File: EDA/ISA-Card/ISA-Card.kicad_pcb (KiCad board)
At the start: 2 copper layers, 138.4 x 98.4 mm, 53 parts, among them U7101 74HCT245, U7102 74HCT244, U7104 74HCT138, U7105 74HCT138, U7106 74LS08, U7107 74LS32, U7108 74LS32, U7109 74HC368, U7110 74HC04, U7111 74HC125, U7112 74HC74, U7113 74HC74, U7114 74HC4024, U7115 74HC4024, U7116 74HC595, U7117 74HC595, U7118 74HC595, U7119 8251, U7120 26LS31, U7121 26LS32, X2 Conn_02x04_Counter_Clockwise, X3 DB15_Female, X5 Conn_02x08_Counter_Clockwise

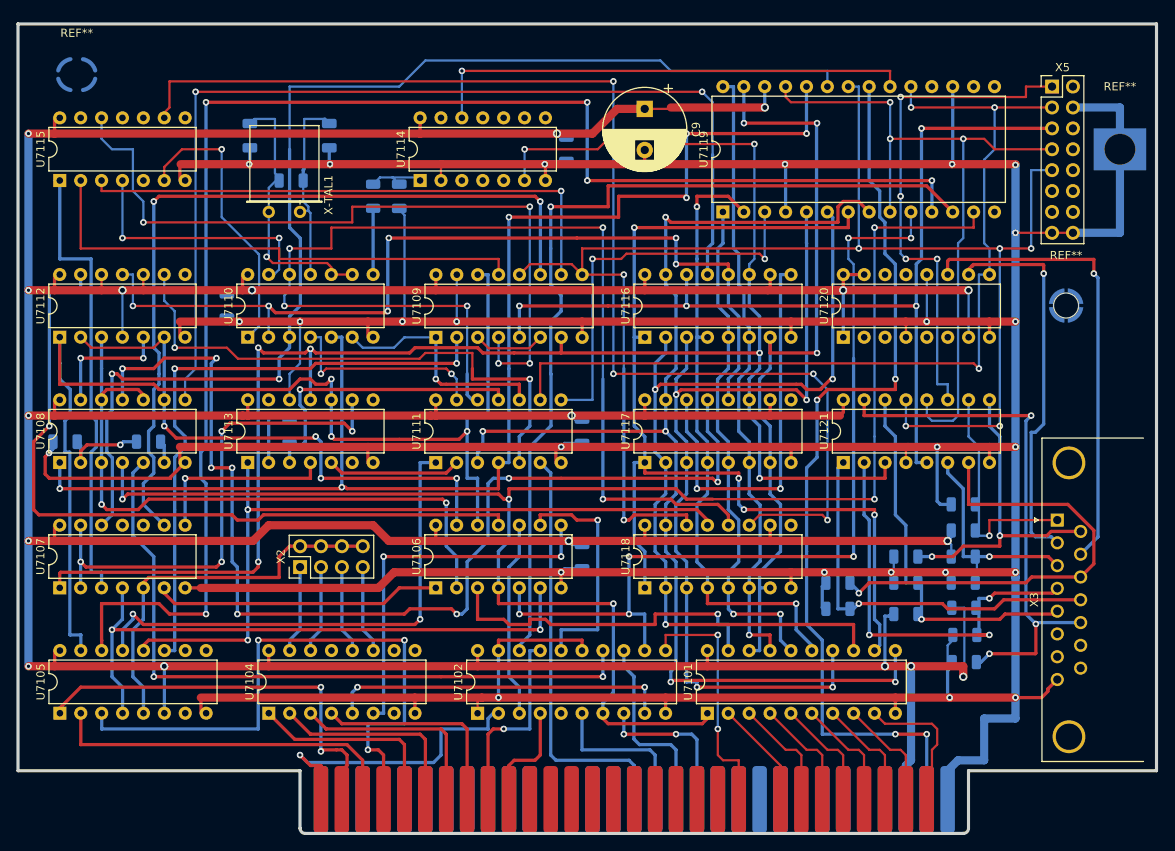
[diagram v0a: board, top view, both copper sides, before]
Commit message: Added test points
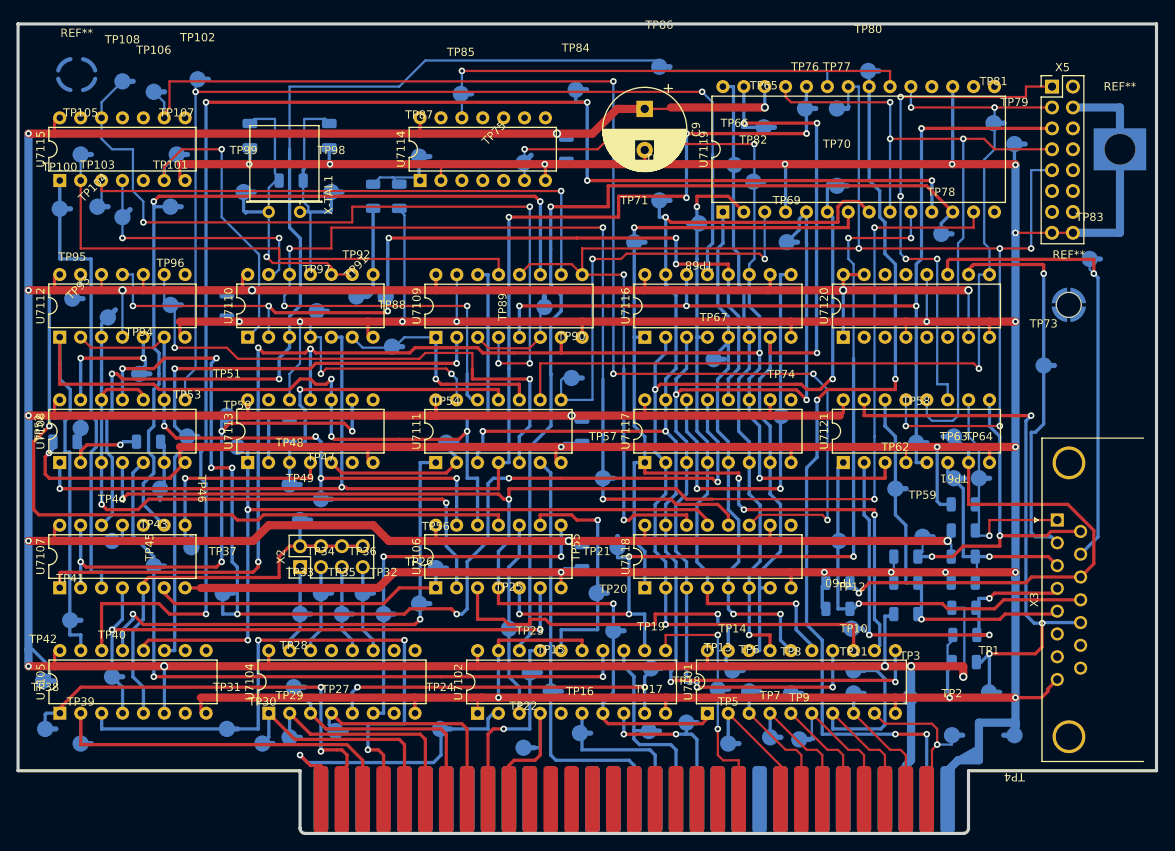
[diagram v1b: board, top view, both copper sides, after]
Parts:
- added TP1: TestPoint, Philips-Shapes:Test Point, F.Cu at (190.4, 132.7)
- added TP10: TestPoint, Philips-Shapes:Test Point, F.Cu at (174.0, 130.0)
- added TP100: TestPoint, Philips-Shapes:Test Point, F.Cu at (77.5, 73.9)
- added TP101: TestPoint, Philips-Shapes:Test Point, F.Cu at (90.9, 73.7)
- added TP102: TestPoint, Philips-Shapes:Test Point, F.Cu at (94.2, 58.2)
- added TP103: TestPoint, Philips-Shapes:Test Point, F.Cu at (82.0, 73.7)
- added TP104: TestPoint, Philips-Shapes:Test Point, F.Cu at (85.1, 74.9)
- added TP105: TestPoint, Philips-Shapes:Test Point, F.Cu at (80.0, 67.3)
- added TP106: TestPoint, Philips-Shapes:Test Point, F.Cu at (88.9, 59.7)
- added TP107: TestPoint, Philips-Shapes:Test Point, F.Cu at (91.7, 67.3)
- added TP108: TestPoint, Philips-Shapes:Test Point, F.Cu at (85.1, 58.4)
- added TP11: TestPoint, Philips-Shapes:Test Point, F.Cu at (174.0, 132.8)
- added TP12: TestPoint, Philips-Shapes:Test Point, F.Cu at (173.7, 125.0)
- added TP13: TestPoint, Philips-Shapes:Test Point, F.Cu at (157.5, 132.3)
- added TP14: TestPoint, Philips-Shapes:Test Point, F.Cu at (159.3, 130.0)
- added TP15: TestPoint, Philips-Shapes:Test Point, F.Cu at (137.2, 132.6)
- added TP16: TestPoint, Philips-Shapes:Test Point, F.Cu at (140.7, 137.7)
- added TP17: TestPoint, Philips-Shapes:Test Point, F.Cu at (149.1, 137.4)
- added TP18: TestPoint, Philips-Shapes:Test Point, F.Cu at (153.7, 136.4)
- added TP19: TestPoint, Philips-Shapes:Test Point, F.Cu at (149.4, 129.8)
- added TP2: TestPoint, Philips-Shapes:Test Point, F.Cu at (185.9, 137.9)
- added TP20: TestPoint, Philips-Shapes:Test Point, F.Cu at (144.8, 125.2)
- added TP21: TestPoint, Philips-Shapes:Test Point, F.Cu at (142.7, 120.7)
- added TP22: TestPoint, Philips-Shapes:Test Point, F.Cu at (133.9, 139.4)
- added TP23: TestPoint, Philips-Shapes:Test Point, F.Cu at (134.6, 130.3)
- added TP24: TestPoint, Philips-Shapes:Test Point, F.Cu at (123.7, 137.2)
- added TP25: TestPoint, Philips-Shapes:Test Point, F.Cu at (132.1, 125.0)
- added TP26: TestPoint, Philips-Shapes:Test Point, F.Cu at (121.2, 121.9)
- added TP27: TestPoint, Philips-Shapes:Test Point, F.Cu at (111.0, 137.4)
- added TP28: TestPoint, Philips-Shapes:Test Point, F.Cu at (105.9, 132.1)
- added TP29: TestPoint, Philips-Shapes:Test Point, F.Cu at (105.4, 138.2)
- added TP3: TestPoint, Philips-Shapes:Test Point, F.Cu at (180.8, 133.3)
- added TP30: TestPoint, Philips-Shapes:Test Point, F.Cu at (102.1, 138.9)
- added TP31: TestPoint, Philips-Shapes:Test Point, F.Cu at (97.8, 137.2)
- added TP32: TestPoint, Philips-Shapes:Test Point, F.Cu at (116.8, 123.2)
- added TP33: TestPoint, Philips-Shapes:Test Point, F.Cu at (106.7, 123.2)
- added TP34: TestPoint, Philips-Shapes:Test Point, F.Cu at (109.2, 120.7)
- added TP35: TestPoint, Philips-Shapes:Test Point, F.Cu at (111.8, 123.2)
- added TP36: TestPoint, Philips-Shapes:Test Point, F.Cu at (114.3, 120.7)
- added TP37: TestPoint, Philips-Shapes:Test Point, F.Cu at (97.3, 120.7)
- added TP38: TestPoint, Philips-Shapes:Test Point, F.Cu at (75.7, 137.2)
- added TP39: TestPoint, Philips-Shapes:Test Point, F.Cu at (80.0, 138.9)
- added TP4: TestPoint, Philips-Shapes:Test Point, F.Cu at (193.5, 137.9)
- added TP40: TestPoint, Philips-Shapes:Test Point, F.Cu at (83.8, 130.8)
- added TP41: TestPoint, Philips-Shapes:Test Point, F.Cu at (78.7, 124.0)
- added TP42: TestPoint, Philips-Shapes:Test Point, F.Cu at (75.4, 131.3)
- added TP43: TestPoint, Philips-Shapes:Test Point, F.Cu at (88.9, 117.3)
- added TP44: TestPoint, Philips-Shapes:Test Point, F.Cu at (83.8, 114.3)
- added TP45: TestPoint, Philips-Shapes:Test Point, F.Cu at (93.5, 115.1)
- added TP46: TestPoint, Philips-Shapes:Test Point, F.Cu at (89.7, 108.0)
- added TP47: TestPoint, Philips-Shapes:Test Point, F.Cu at (109.2, 109.2)
- added TP48: TestPoint, Philips-Shapes:Test Point, F.Cu at (105.4, 107.4)
- added TP49: TestPoint, Philips-Shapes:Test Point, F.Cu at (106.7, 111.8)
- added TP5: TestPoint, Philips-Shapes:Test Point, F.Cu at (158.8, 138.9)
- added TP50: TestPoint, Philips-Shapes:Test Point, F.Cu at (99.1, 102.9)
- added TP51: TestPoint, Philips-Shapes:Test Point, F.Cu at (97.8, 99.1)
- added TP52: TestPoint, Philips-Shapes:Test Point, F.Cu at (80.0, 100.6)
- added TP53: TestPoint, Philips-Shapes:Test Point, F.Cu at (93.0, 101.6)
- added TP54: TestPoint, Philips-Shapes:Test Point, F.Cu at (124.5, 102.4)
- added TP55: TestPoint, Philips-Shapes:Test Point, F.Cu at (145.3, 115.1)
- added TP56: TestPoint, Philips-Shapes:Test Point, F.Cu at (123.2, 117.6)
- added TP57: TestPoint, Philips-Shapes:Test Point, F.Cu at (143.5, 106.7)
- added TP58: TestPoint, Philips-Shapes:Test Point, F.Cu at (181.6, 102.4)
- added TP59: TestPoint, Philips-Shapes:Test Point, F.Cu at (182.4, 113.8)
- added TP6: TestPoint, Philips-Shapes:Test Point, F.Cu at (161.3, 132.6)
- added TP60: TestPoint, Philips-Shapes:Test Point, F.Cu at (172.2, 114.3)
- added TP61: TestPoint, Philips-Shapes:Test Point, F.Cu at (186.2, 101.6)
- added TP62: TestPoint, Philips-Shapes:Test Point, F.Cu at (179.1, 108.0)
- added TP63: TestPoint, Philips-Shapes:Test Point, F.Cu at (186.2, 106.7)
- added TP64: TestPoint, Philips-Shapes:Test Point, F.Cu at (189.2, 106.7)
- added TP65: TestPoint, Philips-Shapes:Test Point, F.Cu at (163.1, 64.0)
- added TP66: TestPoint, Philips-Shapes:Test Point, F.Cu at (159.5, 68.6)
- added TP67: TestPoint, Philips-Shapes:Test Point, F.Cu at (157.0, 92.2)
- added TP68: TestPoint, Philips-Shapes:Test Point, F.Cu at (155.2, 75.7)
- added TP69: TestPoint, Philips-Shapes:Test Point, F.Cu at (165.9, 78.0)
- added TP7: TestPoint, Philips-Shapes:Test Point, F.Cu at (163.8, 138.2)
- added TP70: TestPoint, Philips-Shapes:Test Point, F.Cu at (172.0, 71.1)
- added TP71: TestPoint, Philips-Shapes:Test Point, F.Cu at (147.3, 78.0)
- added TP72: TestPoint, Philips-Shapes:Test Point, F.Cu at (150.4, 72.9)
- added TP73: TestPoint, Philips-Shapes:Test Point, F.Cu at (197.1, 93.0)
- added TP74: TestPoint, Philips-Shapes:Test Point, F.Cu at (165.2, 99.1)
- added TP75: TestPoint, Philips-Shapes:Test Point, F.Cu at (133.9, 68.3)
- added TP76: TestPoint, Philips-Shapes:Test Point, F.Cu at (168.1, 61.7)
- added TP77: TestPoint, Philips-Shapes:Test Point, F.Cu at (172.0, 61.7)
- added TP78: TestPoint, Philips-Shapes:Test Point, F.Cu at (184.7, 77.0)
- added TP79: TestPoint, Philips-Shapes:Test Point, F.Cu at (193.5, 66.0)
- added TP8: TestPoint, Philips-Shapes:Test Point, F.Cu at (166.4, 132.8)
- added TP80: TestPoint, Philips-Shapes:Test Point, F.Cu at (175.8, 57.1)
- added TP81: TestPoint, Philips-Shapes:Test Point, F.Cu at (191.0, 63.5)
- added TP82: TestPoint, Philips-Shapes:Test Point, F.Cu at (161.8, 70.6)
- added TP83: TestPoint, Philips-Shapes:Test Point, F.Cu at (202.7, 80.0)
- added TP84: TestPoint, Philips-Shapes:Test Point, F.Cu at (140.2, 59.4)
- added TP85: TestPoint, Philips-Shapes:Test Point, F.Cu at (126.2, 59.9)
- added TP86: TestPoint, Philips-Shapes:Test Point, F.Cu at (150.4, 56.6)
- added TP87: TestPoint, Philips-Shapes:Test Point, F.Cu at (121.2, 67.6)
- added TP88: TestPoint, Philips-Shapes:Test Point, F.Cu at (117.9, 90.7)
- added TP89: TestPoint, Philips-Shapes:Test Point, F.Cu at (136.4, 85.9)
- added TP9: TestPoint, Philips-Shapes:Test Point, F.Cu at (167.4, 138.4)
- added TP90: TestPoint, Philips-Shapes:Test Point, F.Cu at (139.7, 94.5)
- added TP91: TestPoint, Philips-Shapes:Test Point, F.Cu at (117.1, 84.6)
- added TP92: TestPoint, Philips-Shapes:Test Point, F.Cu at (113.5, 84.6)
- added TP93: TestPoint, Philips-Shapes:Test Point, F.Cu at (83.3, 87.1)
- added TP94: TestPoint, Philips-Shapes:Test Point, F.Cu at (87.1, 94.0)
- added TP95: TestPoint, Philips-Shapes:Test Point, F.Cu at (79.0, 84.8)
- added TP96: TestPoint, Philips-Shapes:Test Point, F.Cu at (90.9, 85.6)
- added TP97: TestPoint, Philips-Shapes:Test Point, F.Cu at (108.7, 86.4)
- added TP98: TestPoint, Philips-Shapes:Test Point, F.Cu at (110.5, 71.9)
- added TP99: TestPoint, Philips-Shapes:Test Point, F.Cu at (99.8, 71.9)
- moved REF** 0.34 mm to (200.2, 85.6)
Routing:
- net /D5: track 13.9 -> 31.1 mm
- net Net-(C5-Pad2): track 23.7 -> 29.8 mm
- net VCC: track 726.7 -> 732.5 mm
- net Net-(C6-Pad2): track 32.9 -> 38.4 mm
- net Net-(U7109-Pad4): track 91.2 -> 96.7 mm
- net /A9: track 13.5 -> 18.8 mm
- net /MDB3: track 106.3 -> 111.1 mm
- net /MDB4: track 106.4 -> 111.1 mm
- net Net-(R3-Pad2): track 8.05 -> 12.5 mm
- net /Attention-: track 65.1 -> 69.5 mm
- net Net-(TP37-Pad1): track 133.9 -> 138.2 mm
- net /D4: track 13.9 -> 17.9 mm
- net /Data-: track 57.5 -> 61.5 mm
- net /A4: track 24.8 -> 28.8 mm
- net /A6: track 25.5 -> 29.5 mm
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
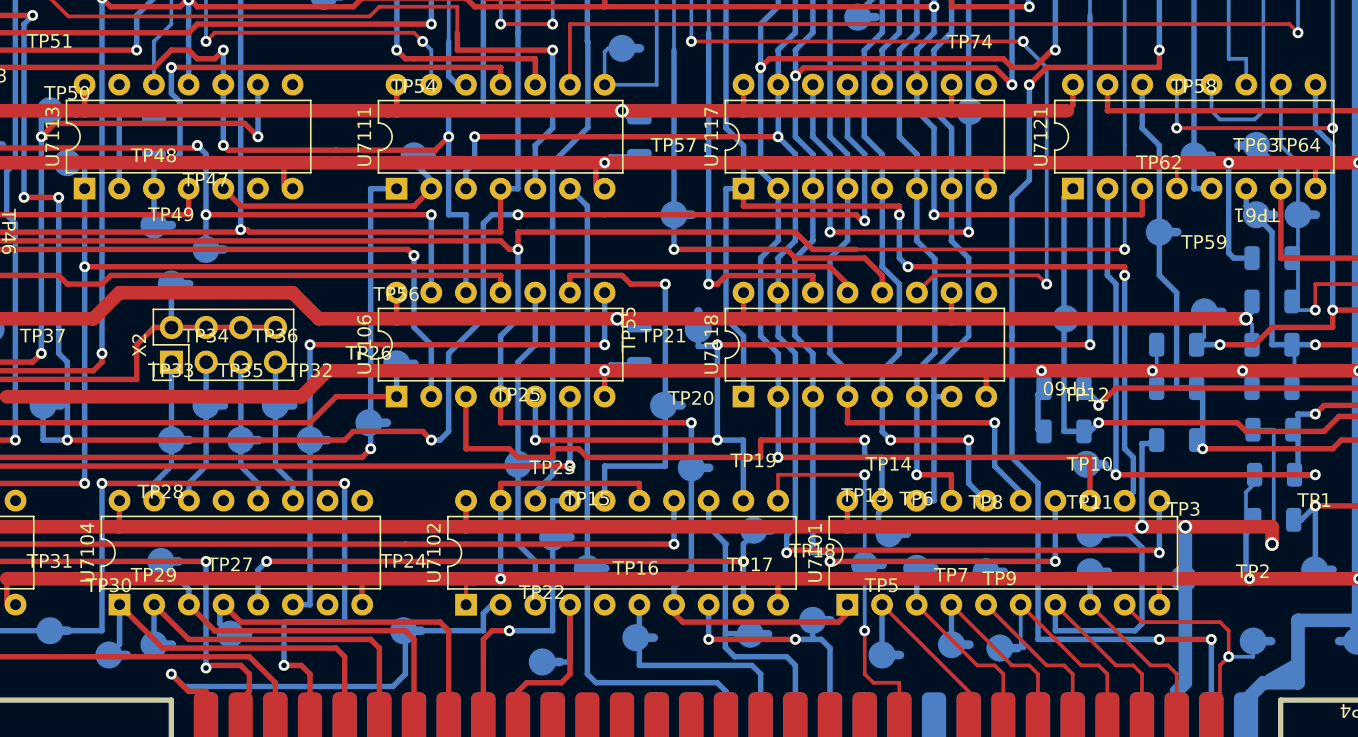
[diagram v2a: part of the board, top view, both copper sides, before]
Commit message: Fixed missed connection on 7113 Pin 13
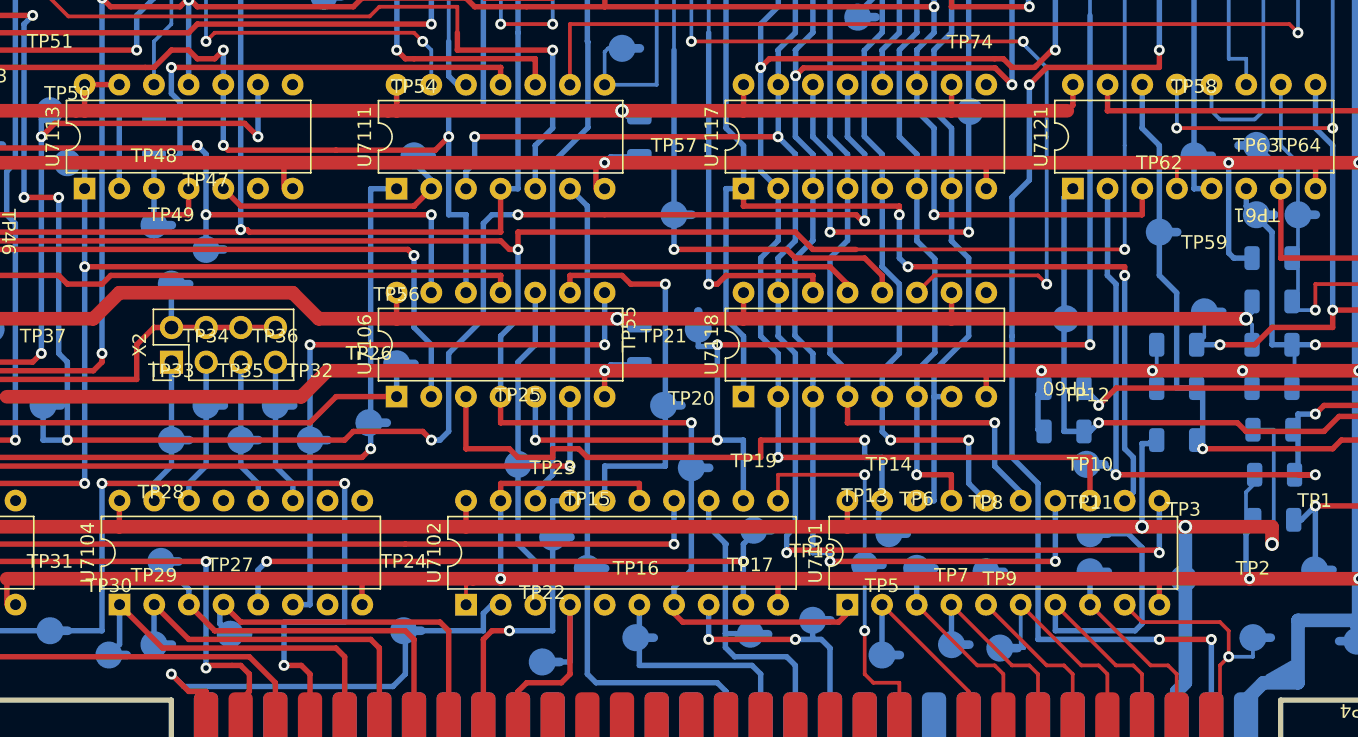
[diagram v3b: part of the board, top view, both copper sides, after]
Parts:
- moved TP2 0.25 mm to (185.9, 137.7)
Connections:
- net /Data Clock HV renamed /CLKp3
- net /Port Selection renamed /IOSEL
- net Net-(R4-Pad2) renamed /DMA_READ
- net Net-(TP19-Pad1) renamed /AENb
- net Net-(TP20-Pad1) renamed /~{RD}
- net Net-(TP21-Pad1) renamed /A9b
- net Net-(TP25-Pad1) renamed /A8b
- net Net-(TP40-Pad1) renamed /IOACT
- net Net-(TP43-Pad1) renamed /DMA_ACK
- net Net-(TP55-Pad1) renamed /~{WR}
- net Net-(U7102-Pad18) renamed /A0b
- net Net-(U7108-Pad1) renamed /~{DTR}
- net Net-(U7114-Pad12) renamed /CLKp0
- U7113 pad 13: unconnected-(U7113-Pad13) -> VCC
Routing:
- net VCC: track 732.5 -> 735.0 mm

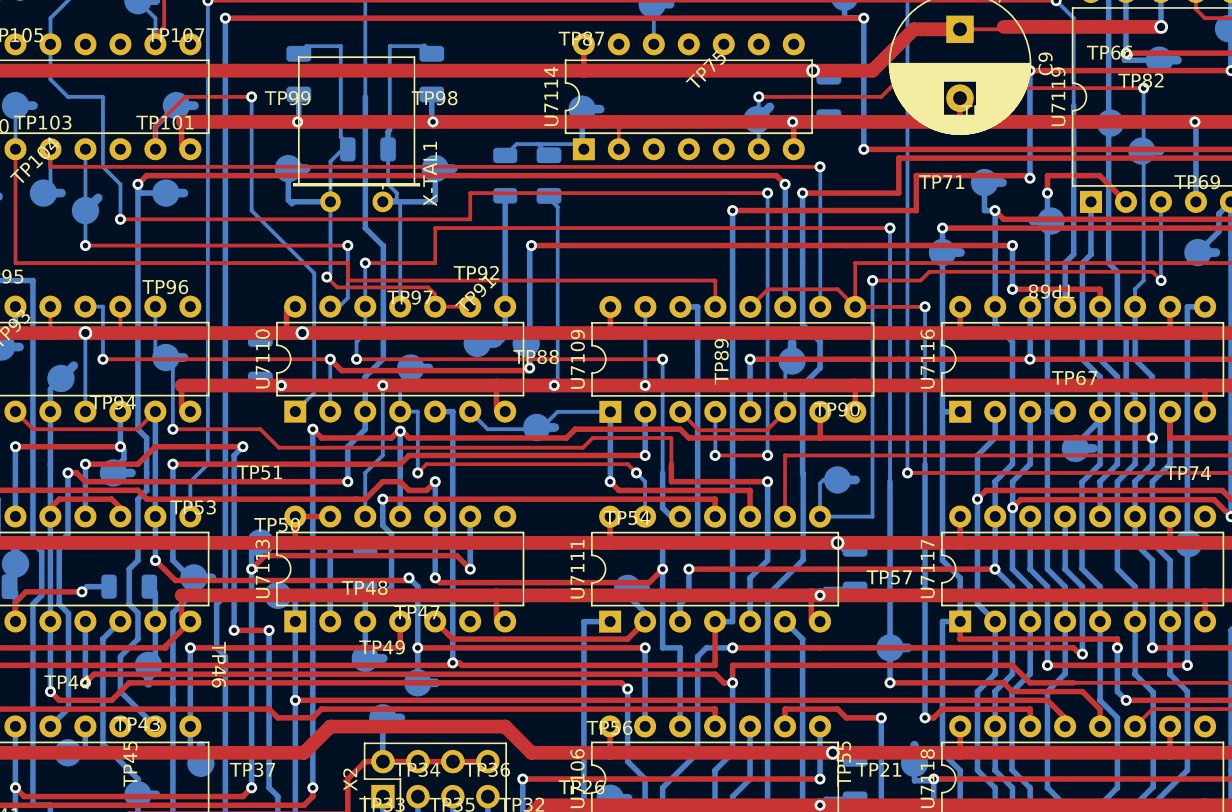
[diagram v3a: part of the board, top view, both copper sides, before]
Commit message: All nets checked and annotated for number of test pads Three nets are missing test pads, though one is connecting a two pins through a resistor and seems harmless. The othersare going to the drive interfaces. \ \ There is one net with two pads. It should likely be split with one pad going to one of the nets missing one.
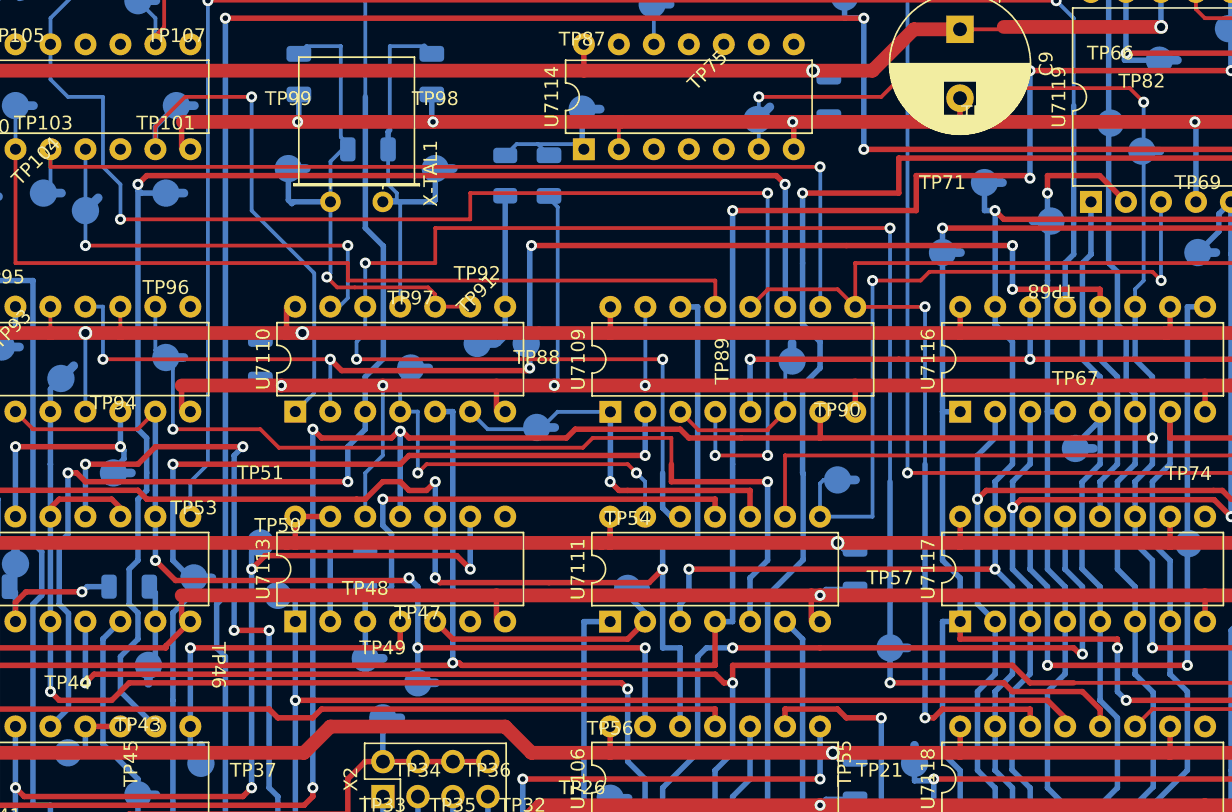
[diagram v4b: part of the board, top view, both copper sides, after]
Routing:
- net Net-(TP44-Pad1): track 3.02 -> 5.56 mm
- net /CLKp3: track 216.6 -> 216.0 mm
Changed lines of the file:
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@@
   (segment (start 108.094492 90.949492) (end 107.950564 90.949492) (width 0.4) (layer "F.Cu") (net 95))
   (segment (start 108.585 91.44) (end 108.094492 90.949492) (width 0.4) (layer "F.Cu") (net 95))
+  (segment (start 160.909 66.04) (end 161.925 67.056) (width 0.275) (layer "F.Cu") (net 95))
   (segment (start 77.465 120.005) (end 77.465 118.218964) (width 0.4) (layer "F.Cu") (net 95))
   (segment (start 177.8 106.68) (end 177.815 106.665) (width 0.4) (layer "F.Cu") (net 95))
-  (segment (start 152.4 66.04) (end 161.925 66.04) (width 0.275) (layer "F.Cu") (net 95))
   (segment (start 144.78 64.77) (end 152.4 64.77) (width 0.275) (layer "F.Cu") (net 95))
   (segment (start 133.985 66.675) (end 142.875 66.675) (width 0.275) (layer "F.Cu") (net 95))
@@
   (segment (start 120.65 90.805) (end 120.015 91.44) (width 0.4) (layer "F.Cu") (net 95))
   (segment (start 101.6 117.475) (end 101.6 116.84) (width 0.4) (layer "F.Cu") (net 95))
+  (segment (start 152.4 66.04) (end 160.909 66.04) (width 0.275) (layer "F.Cu") (net 95))
   (segment (start 162.56 106.68) (end 177.8 106.68) (width 0.4) (layer "F.Cu") (net 95))
   (segment (start 128.27 90.805) (end 120.65 90.805) (width 0.4) (layer "F.Cu") (net 95))
@@
   (via (at 101.6 90.805) (size 0.8) (drill 0.4) (layers "F.Cu" "B.Cu") (net 95))
   (via (at 162.56 91.44) (size 0.8) (drill 0.4) (layers "F.Cu" "B.Cu") (net 95))
-  (via (at 161.925 66.04) (size 0.8) (drill 0.4) (layers "F.Cu" "B.Cu") (net 95))
+  (via (at 161.925 67.056) (size 0.8) (drill 0.4) (layers "F.Cu" "B.Cu") (net 95))
   (via (at 101.6 116.84) (size 0.8) (drill 0.4) (layers "F.Cu" "B.Cu") (net 95))
   (via (at 107.950564 90.949492) (size 0.8) (drill 0.4) (layers "F.Cu" "B.Cu") (net 95))
@@
   (segment (start 161.305 97.145) (end 161.305 94.63) (width 0.4) (layer "B.Cu") (net 95))
   (segment (start 161.305 85.71) (end 161.305 81.915) (width 0.4) (layer "B.Cu") (net 95))
-  (segment (start 161.925 66.04) (end 161.925 80.01) (width 0.275) (layer "B.Cu") (net 95))
   (segment (start 161.305 80.66) (end 161.305 81.915) (width 0.275) (layer "B.Cu") (net 95))
   (segment (start 107.945 90.955056) (end 107.945 97.145) (width 0.4) (layer "B.Cu") (net 95))
@@
   (segment (start 107.950564 90.949492) (end 107.945 90.955056) (width 0.4) (layer "B.Cu") (net 95))
   (segment (start 161.29 80.645) (end 161.305 80.66) (width 0.275) (layer "B.Cu") (net 95))
+  (segment (start 161.925 80.01) (end 161.925 67.056) (width 0.275) (layer "B.Cu") (net 95))
   (segment (start 161.305 97.145) (end 161.305 99.075) (width 0.4) (layer "B.Cu") (net 95))
   (segment (start 156.21 64.77) (end 168.275 64.77) (width 0.4) (layer "F.Cu") (net 96))
@@
   (segment (start 97.155 74.93) (end 97.155 66.675) (width 0.275) (layer "B.Cu") (net 173))
   (segment (start 90.17 68.834) (end 90.17 70.475) (width 0.4) (layer "B.Cu") (net 173))
+  (segment (start 87.625 112.385) (end 85.085 112.385) (width 0.4) (layer "F.Cu") (net 174))
   (segment (start 85.085 114.0256) (end 84.8106 114.3) (width 0.4) (layer "B.Cu") (net 174))
   (segment (start 85.085 112.385) (end 85.085 114.0256) (width 0.4) (layer "B.Cu") (net 174))
